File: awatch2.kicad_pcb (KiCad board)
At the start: 4 copper layers, 86 x 46 mm, 166 parts, among them J101 Conn_01x02, J102 Conn_01x02, J103 Conn_01x02, J104 Conn_01x02, J301 Conn_01x02, J801 Molex 1050170001, J802 Conn_01x06, Q701 FDV301N, SW101 B3S-1000, SW102 B3S-1000, SW103 B3S-1000, SW104 B3S-1000, U1 nRF52840, U301 MAX14690, U401 W25Q128JVPIQTR, U501 BMM150, U502 APDS-9306-065, U503 BMI160, U504 BMP388, U601 SPK0641HT4H-1, U701 AYF531035 (LS013B7DH05), U801 AT93C46DN-SH-T, U802 MCP1703A-3302_SOT223, U803 FT2232HL, U901 DRV2604, X1 ABM11W-32.0000MHZ-8-B1U-T3, Y801 FH1200004

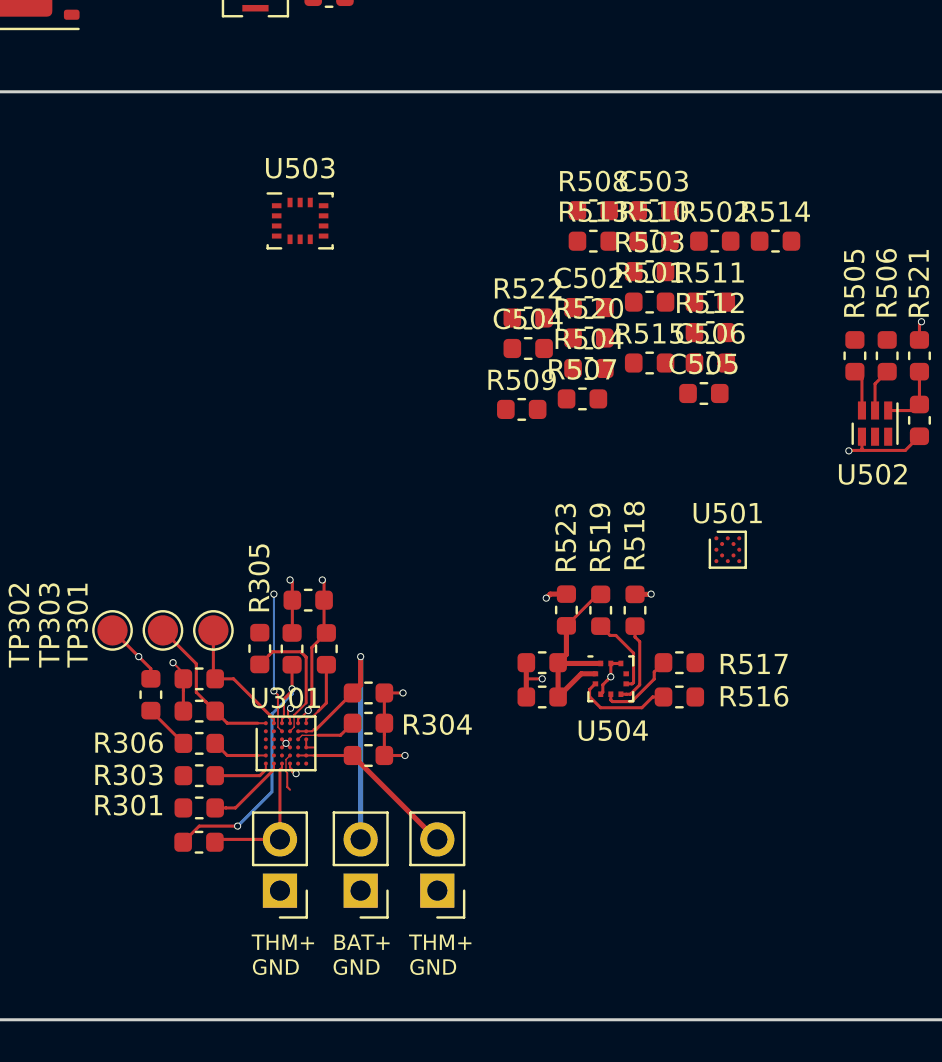
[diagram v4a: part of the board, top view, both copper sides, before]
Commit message: IMU and magnetometer placed and routed
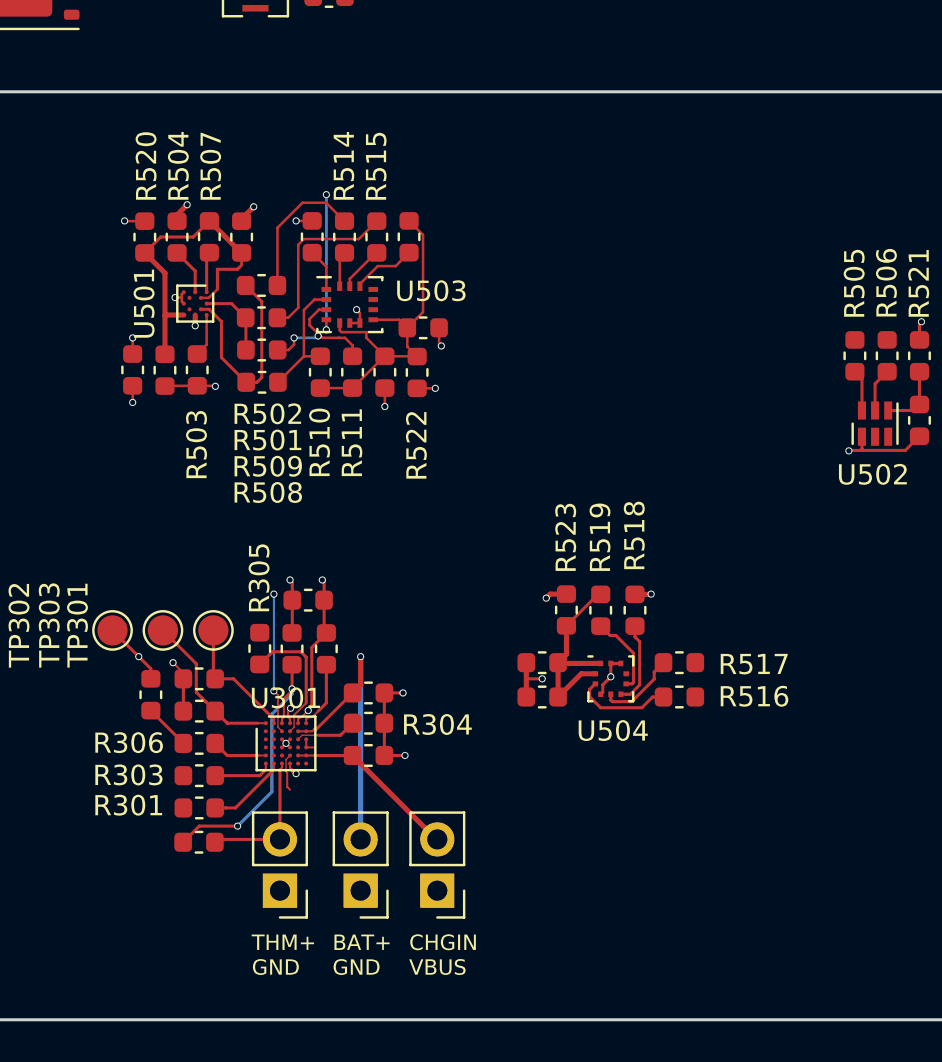
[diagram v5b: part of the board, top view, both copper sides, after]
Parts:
- moved U501 29.1 mm to (92.2, 48.5), turned to 270 degrees
- moved R503 22.9 mm to (92.3, 51.8), turned to 90 degrees
- moved R520 22.6 mm to (89.7, 45.2), turned to 90 degrees
- moved R502 22.6 mm to (95.5, 47.6)
- moved R504 21.4 mm to (91.3, 45.2), turned to 270 degrees
- moved R514 21.4 mm to (99.6, 45.2), turned to 270 degrees
- moved C502 21.2 mm to (90.7, 51.8), turned to 270 degrees
- moved C503 20.5 mm to (94.5, 45.2), turned to 90 degrees
- moved R507 20.2 mm to (92.9, 45.2), turned to 90 degrees
- moved C504 19.6 mm to (89.1, 51.8), turned to 270 degrees
- moved R501 19.3 mm to (95.5, 49.2)
- moved R508 18.5 mm to (95.5, 52.4), turned to 180 degrees
- moved R511 18.1 mm to (100.0, 51.9), turned to 90 degrees
- moved R510 17.8 mm to (98.4, 51.9), turned to 90 degrees
- moved C506 16.1 mm to (101.6, 51.9), turned to 270 degrees
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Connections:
- net Net-(C502-Pad1) renamed /Sensors/MAG_VDD
- net Net-(C505-Pad1) renamed /Sensors/IMU_VDD
- net Net-(R501-Pad1) renamed /Sensors/MAG_SCK
- net Net-(R502-Pad1) renamed /Sensors/MAG_SDI
- net Net-(R504-Pad2) renamed /Sensors/MAG_SDO
- net Net-(R507-Pad1) renamed /Sensors/MAG_PS
- net Net-(R508-Pad1) renamed /Sensors/IMUM_SDA
- net Net-(R509-Pad1) renamed /Sensors/IMUM_SCK
- net Net-(R512-Pad1) renamed /Sensors/IMU_CSB
- net Net-(R513-Pad2) renamed /Sensors/IMU_SDO
- net Net-(R514-Pad2) renamed /Sensors/IMU_SDA
- net Net-(R515-Pad2) renamed /Sensors/IMU_SCK
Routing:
- net /Sensors/MAG_VDD: track 0.00 -> 20.4 mm
- net /Sensors/IMU_VDD: track 0.00 -> 18.1 mm
- net GND: track 94.3 -> 105.1 mm, vias 41 -> 51
- net /Sensors/MAG_SDI: track 0.00 -> 10.6 mm
- net /Sensors/SENS_SCL: track 0.00 -> 8.74 mm
- net /Sensors/SENS_IMU_INT: track 0.00 -> 7.20 mm, vias 0 -> 2
- net /Sensors/IMUM_SCK: track 0.00 -> 7.14 mm, vias 0 -> 2
- net /Sensors/SENS_SDA: track 0.00 -> 7.08 mm
- net /Sensors/IMUM_SDA: track 0.00 -> 6.25 mm
- net /Sensors/MAG_SCK: track 0.00 -> 3.83 mm
- net /Sensors/IMU_CSB: track 0.00 -> 3.19 mm
- net +2V8: track 32.4 -> 35.1 mm, vias 10 -> 13
- net /Sensors/MAG_SDO: track 0.00 -> 2.32 mm
- net /Sensors/IMU_SCK: track 0.00 -> 2.23 mm
- net Net-(R503-Pad2): track 0.00 -> 2.13 mm
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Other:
- net class Magnetometer 4/4 added: clearance 0.1016, trace_width 0.1016, via_dia 0.3556, via_drill 0.254
- board text added: "CHGIN VBUS"

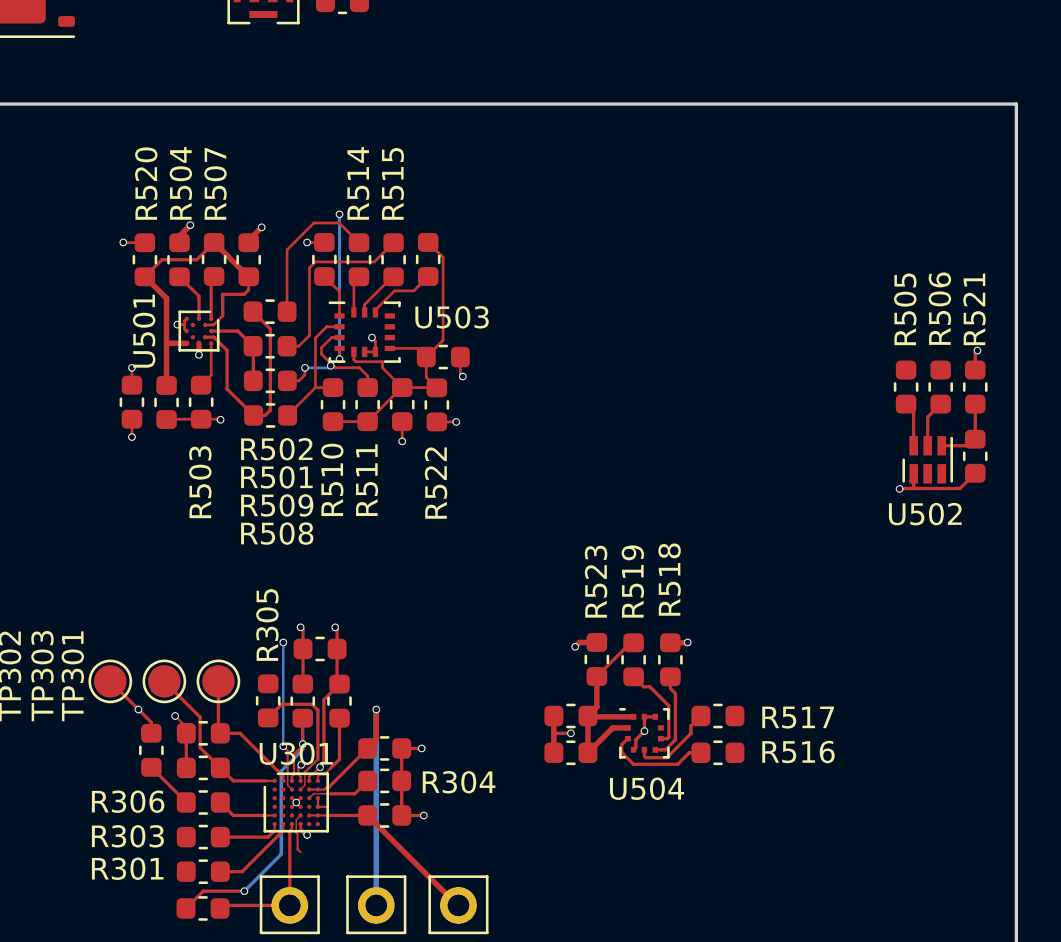
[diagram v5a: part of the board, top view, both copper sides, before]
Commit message: placed and routed all four sensors
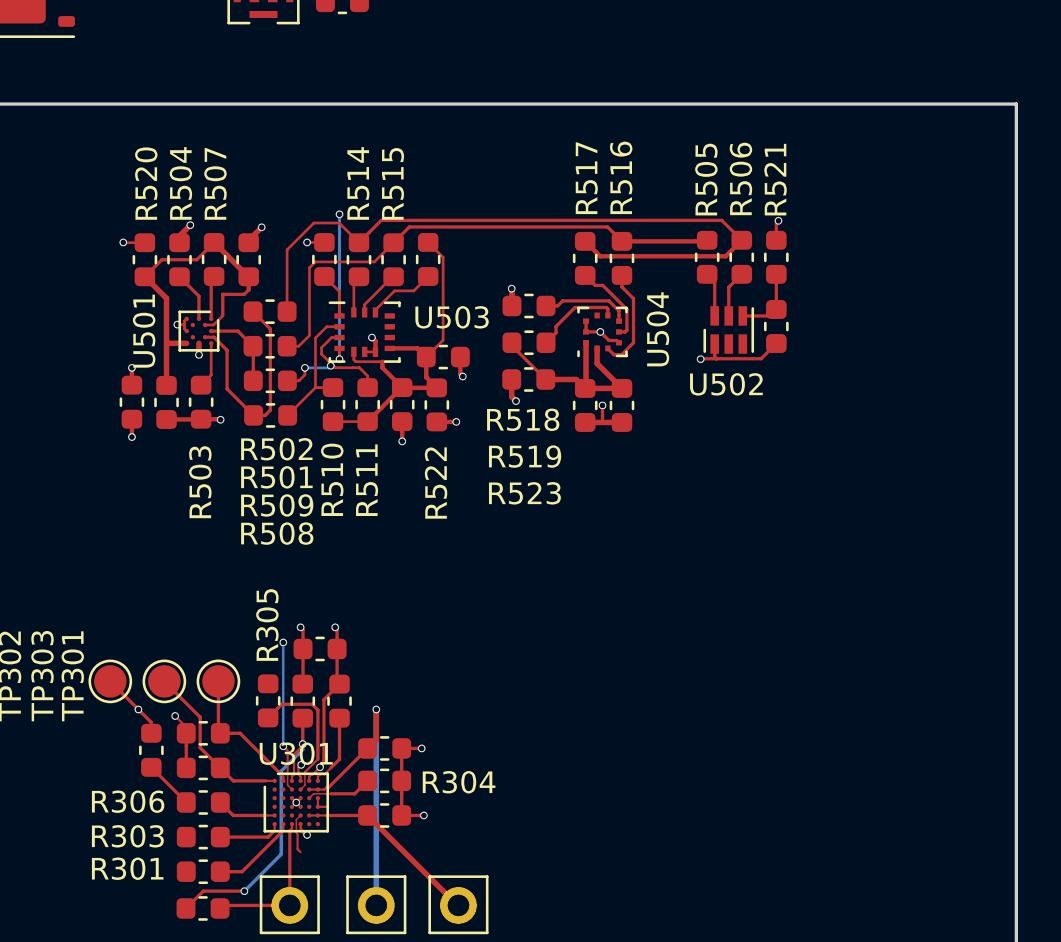
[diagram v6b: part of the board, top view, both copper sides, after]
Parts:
- moved R516 23.3 mm to (111.8, 45.1), turned to 90 degrees
- moved R517 22.0 mm to (110.1, 45.1), turned to 90 degrees
- moved U504 18.7 mm to (110.9, 48.5), turned to 90 degrees
- moved R518 17.6 mm to (107.5, 47.3), turned to 0 degrees
- moved C508 16.2 mm to (111.8, 51.9), turned to 270 degrees
- moved R519 15.4 mm to (107.5, 49.0), turned to 180 degrees
- moved C507 14.4 mm to (110.1, 51.9), turned to 270 degrees
- moved R523 13.3 mm to (107.4, 50.7), turned to 180 degrees
- moved R505 11.0 mm to (115.7, 45.1)
- moved R506 11.0 mm to (117.3, 45.1)
- moved U502 11.0 mm to (116.7, 48.5)
- moved C501 11.0 mm to (118.9, 48.3)
- moved R521 11.0 mm to (118.9, 45.1)
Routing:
- net /Sensors/SENS_SDA: track 7.08 -> 33.4 mm
- net /Sensors/SENS_SCL: track 8.74 -> 23.8 mm

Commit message: vibe, mic, display P&R
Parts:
- moved J101 80.9 mm to (138.2, 67.7), turned to 180 degrees
- moved R905 53.5 mm to (135.6, 68.1), turned to 270 degrees
- moved U901 52.2 mm to (133.4, 65.3)
- moved R902 52.1 mm to (129.2, 68.1), turned to 270 degrees
- moved R901 51.3 mm to (130.8, 68.1), turned to 270 degrees
- moved C901 50.8 mm to (132.4, 68.1), turned to 270 degrees
- moved C902 50.3 mm to (134.0, 68.1), turned to 270 degrees
- moved R602 48.8 mm to (139.2, 59.2)
- moved C601 48.7 mm to (139.2, 57.6)
- moved U601 47.7 mm to (135.4, 57.8)
- moved R904 47.3 mm to (130.0, 65.7)
- moved D703 46.5 mm to (142.6, 45.2), turned to 270 degrees
- moved R601 46.3 mm to (139.2, 56.0), turned to 180 degrees
- moved C903 46.0 mm to (130.0, 62.5), turned to 180 degrees
- moved R706 44.7 mm to (141.0, 49.3), turned to 90 degrees
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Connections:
- net Net-(C901-Pad1) renamed /Vibrate motor driver/VIBE_VDD
- net Net-(C903-Pad1) renamed /Vibrate motor driver/VIBE_REG
- net Net-(R901-Pad1) renamed /Vibrate motor driver/VIBE_SCL_IN
- net Net-(R902-Pad1) renamed /Vibrate motor driver/VIBE_SDA_IN
- net Net-(R903-Pad2) renamed /Vibrate motor driver/VIBE_EN
- net Net-(R904-Pad2) renamed /Vibrate motor driver/VIBE_IN
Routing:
- net GND: track 105.1 -> 135.4 mm, vias 51 -> 64
- net Net-(D701-Pad1): track 0.00 -> 13.7 mm
- net +2V8: track 35.1 -> 46.9 mm, vias 13 -> 15
- net /Microphone/MIC_nSTBY: track 0.00 -> 9.81 mm
- net /Vibrate motor driver/VIBE_OUT-: track 0.00 -> 5.48 mm
- net Net-(R702-Pad1): track 0.00 -> 5.35 mm
- net Net-(R703-Pad1): track 0.00 -> 5.13 mm
- net /Vibrate motor driver/VIBE_SDA_IN: track 0.00 -> 5.04 mm
- net /Vibrate motor driver/VIBE_VDD: track 0.00 -> 4.96 mm
- net Net-(R701-Pad2): track 0.00 -> 4.89 mm
- net Net-(C601-Pad1): track 0.00 -> 4.66 mm
- net /Vibrate motor driver/VIBE_OUT+: track 0.00 -> 4.47 mm
- net /Microphone/MIC_DIN: track 0.00 -> 3.97 mm
- net Net-(D701-Pad2): track 0.00 -> 3.78 mm
- net /Microphone/MIC_CLK: track 0.00 -> 3.76 mm
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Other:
- board size 86 x 46 mm -> 102.4 x 46.1 mm
- net class Vibe 2.75 added: clearance 0.0762, trace_width 0.06985, via_dia 0.3556, via_drill 0.254
- board text added: "VIBE+ VIBE-"

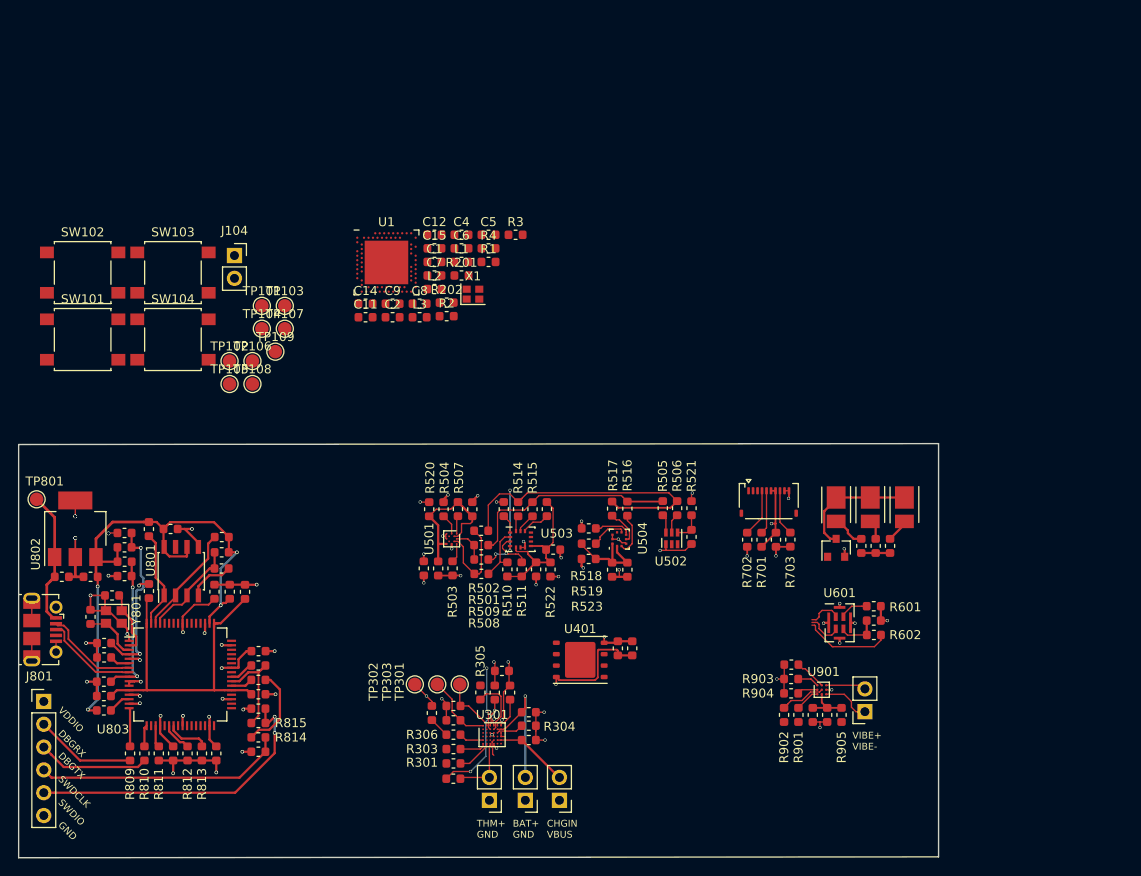
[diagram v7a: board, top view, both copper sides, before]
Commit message: relative placement and routing for nRF52840
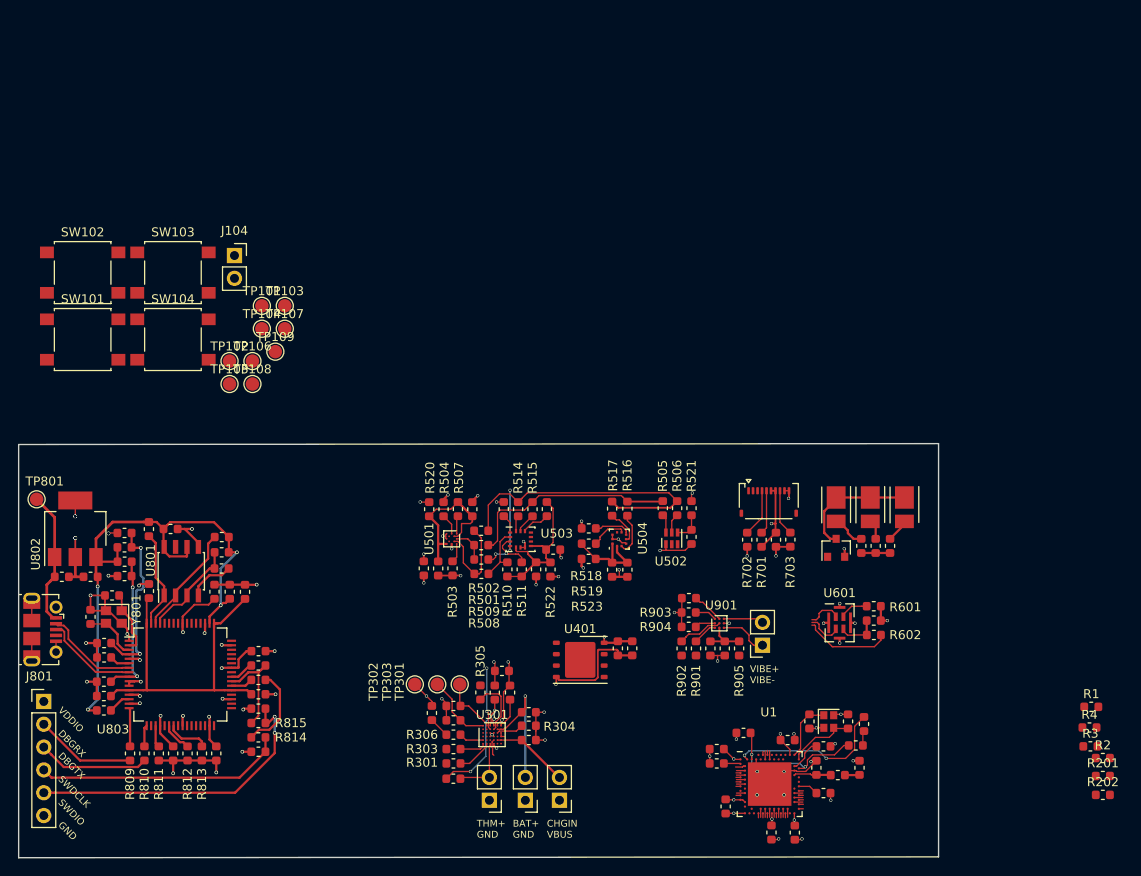
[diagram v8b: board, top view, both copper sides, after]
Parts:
- added C3: 1.0pF NP0, Capacitor_SMD:C_0603_1608Metric, F.Cu at (132.8, 74.0)
- moved R202 91.3 mm to (164.7, 77.0)
- moved R201 90.6 mm to (164.7, 74.9)
- moved R2 88.1 mm to (164.7, 72.9)
- moved R3 85.7 mm to (163.3, 71.6)
- moved R4 85.6 mm to (163.2, 69.5)
- moved R1 83.4 mm to (163.4, 67.2)
- moved C4 74.0 mm to (137.6, 74.0), turned to 90 degrees
- moved C9 72.6 mm to (133.6, 76.8), turned to 180 degrees
- moved C7 72.5 mm to (127.8, 81.2), turned to 270 degrees
- moved C8 72.2 mm to (130.4, 81.2), turned to 270 degrees
- moved U1 72.0 mm to (127.6, 75.8)
- moved L1 70.8 mm to (135.2, 74.8), turned to 180 degrees
- moved C11 69.9 mm to (133.6, 71.6), turned to 180 degrees
- moved C6 68.7 mm to (122.7, 78.3), turned to 270 degrees
- moved C12 68.6 mm to (129.6, 70.9)
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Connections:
- C4 pad 1: Net-(C4-Pad1) -> /nRF52840/NRF_ANT
- L1 pad 2: Net-(C4-Pad1) -> Net-(C3-Pad1)
- U1 pad H23: Net-(C4-Pad1) -> Net-(C3-Pad1)
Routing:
- net GND: track 135.4 -> 158.2 mm, vias 64 -> 80
- net Net-(L2-Pad2): track 0.00 -> 17.8 mm, vias 0 -> 2
- net Net-(C15-Pad2): track 0.00 -> 17.1 mm, vias 0 -> 2
- net +2V8: track 46.9 -> 57.0 mm, vias 15 -> 20
- net Net-(C2-Pad1): track 0.00 -> 7.65 mm
- net Net-(C1-Pad1): track 0.00 -> 6.85 mm
- net Net-(C3-Pad1): track 0.00 -> 4.15 mm
- net Net-(C11-Pad2): track 0.00 -> 3.68 mm
- net Net-(C9-Pad2): track 0.00 -> 2.26 mm
- net Net-(C5-Pad2): track 0.00 -> 1.87 mm
- net Net-(L2-Pad1): track 0.00 -> 1.65 mm
- net /nRF52840/NRF_ANT: track 0.00 -> 1.64 mm
- net /Microphone/MIC_CLK: track 3.76 -> 4.85 mm
- net /nRF52840/BTN_CENTER: track 0.00 -> 0.95 mm
- net /PMIC/PMIC_INTn: track 6.97 -> 7.92 mm
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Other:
- net class NRF 3/3 added: clearance 0.1016, trace_width 0.1016, via_dia 0.3556, via_drill 0.254
